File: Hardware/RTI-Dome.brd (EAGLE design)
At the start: 80 x 71.1 mm, 49 parts, among them IC1 24AA128ST, IC2 74LVC244, IC3 FT232RL, IC4 74ABT244, X13 PN61729-S

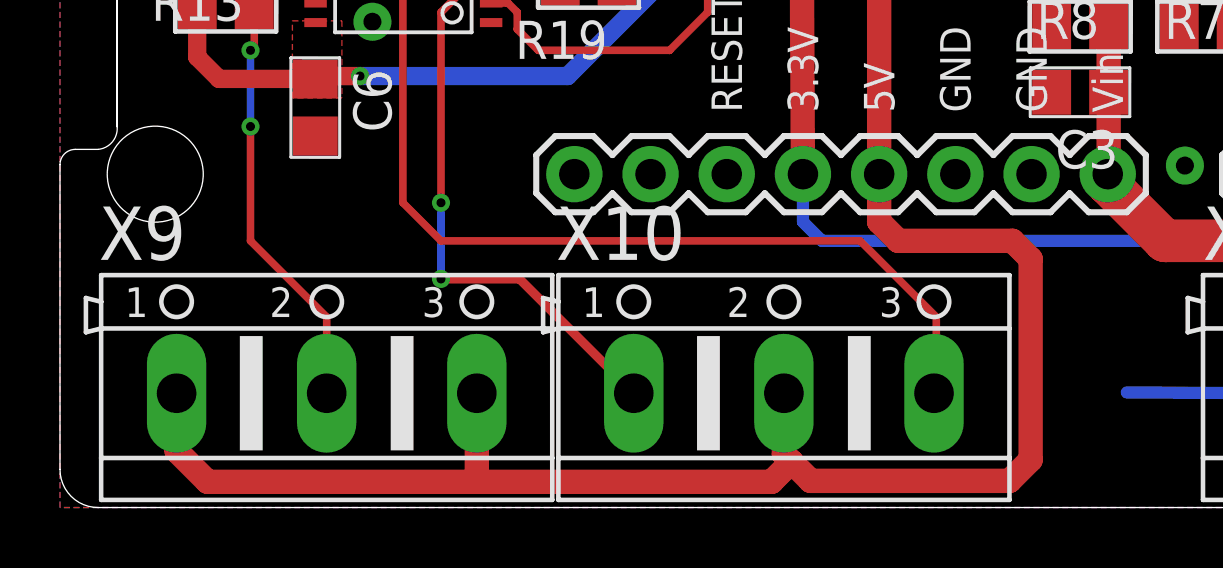
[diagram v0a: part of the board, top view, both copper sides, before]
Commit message: fix the stepper connection to match the TB6600 and work with the ISD02/04/08 controller with the same settings
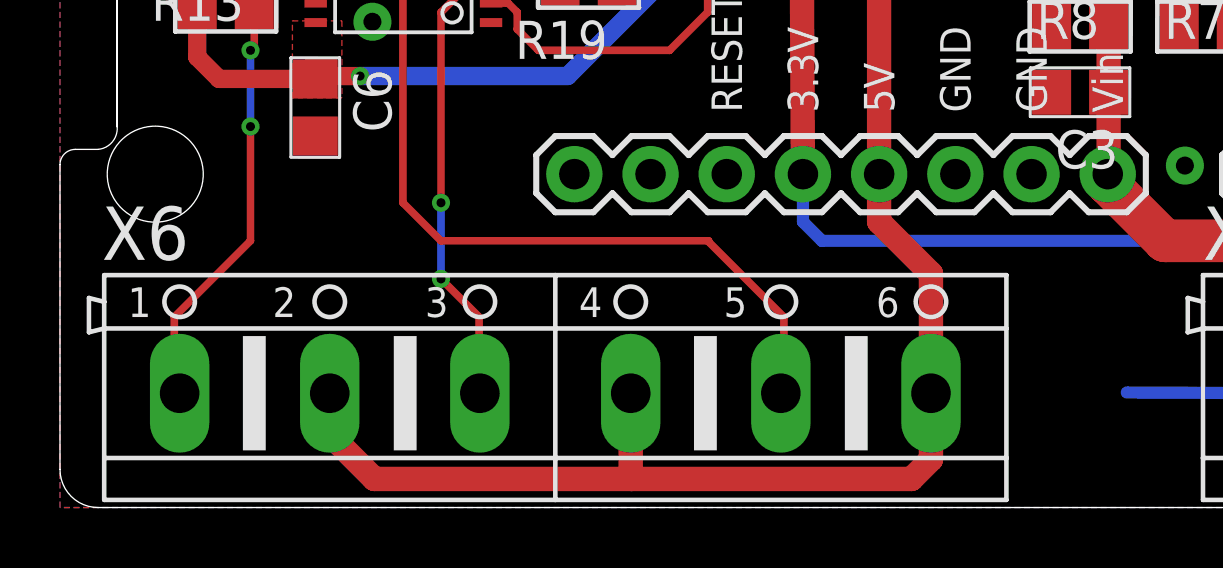
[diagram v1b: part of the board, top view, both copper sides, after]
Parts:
- removed X10, X9: (no value), con-ptr500:AK500/3
- added X6: (no value), con-ptr500:AK500/6
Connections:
- net M_DIR_5V: now also X6.3; no longer X10.1
- net M_EN_5V: now also X6.1; no longer X9.2
- net M_STEP_5V: now also X6.5; no longer X10.3
- net VCC: now also X6.2, X6.4, X6.6; no longer X10.2, X9.1, X9.3
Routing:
- net VCC: track 178.2 -> 162.8 mm
- net M_STEP_5V: track 34.9 -> 29.9 mm
- net M_DIR_5V: track 21.3 -> 17.6 mm
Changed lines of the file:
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@@
 <attribute name="OC_FARNELL" value="unknown" x="6.35" y="66.04" size="1.778" layer="27" rot="R180" display="off"/>
-</element>
-<element name="X9" library="con-ptr500" package="AK500/3" value="" x="8.89" y="3.81">
-<attribute name="MPN" value="" x="8.89" y="3.81" size="1.778" layer="27" display="off"/>
-<attribute name="MF" value="" x="8.89" y="3.81" size="1.778" layer="27" display="off"/>
-<attribute name="OC_NEWARK" value="unknown" x="8.89" y="3.81" size="1.778" layer="27" display="off"/>
-<attribute name="OC_FARNELL" value="unknown" x="8.89" y="3.81" size="1.778" layer="27" display="off"/>
-</element>
-<element name="X10" library="con-ptr500" package="AK500/3" value="" x="24.13" y="3.81">
-<attribute name="MPN" value="" x="24.13" y="3.81" size="1.778" layer="27" display="off"/>
-<attribute name="MF" value="" x="24.13" y="3.81" size="1.778" layer="27" display="off"/>
-<attribute name="OC_NEWARK" value="unknown" x="24.13" y="3.81" size="1.778" layer="27" display="off"/>
-<attribute name="OC_FARNELL" value="unknown" x="24.13" y="3.81" size="1.778" layer="27" display="off"/>
 </element>
 <element name="X11" library="con-ptr500" package="AK500/2" value="" x="60.96" y="3.81">
@@
 <element name="C9" library="rti" package="C0805" value="100nF" x="60.833" y="24.73325" rot="R270"/>
 <element name="R21" library="rti" package="R0805" value="4.7K" x="39.6875" y="43.18" rot="R270"/>
+<element name="X6" library="con-ptr500" package="AK500/6" value="" x="16.51" y="3.81">
+<attribute name="OC_NEWARK" value="unknown" x="16.51" y="3.81" size="1.778" layer="27" display="off"/>
+<attribute name="OC_FARNELL" value="unknown" x="16.51" y="3.81" size="1.778" layer="27" display="off"/>
+<attribute name="MF" value="" x="16.51" y="3.81" size="1.778" layer="27" display="off"/>
+<attribute name="MPN" value="" x="16.51" y="3.81" size="1.778" layer="27" display="off"/>
+</element>
 </elements>
 <signals>
@@
 <signal name="M_STEP_5V">
 <contactref element="R13" pad="1"/>
-<contactref element="X10" pad="3"/>
 <contactref element="IC4" pad="P$16"/>
 <wire x1="6.44275" y1="18.76425" x2="8.51925" y2="18.76425" width="0.254" layer="1"/>
@@
 <wire x1="11.43" y1="17.78" x2="11.43" y2="10.16" width="0.254" layer="1"/>
 <wire x1="11.43" y1="10.16" x2="12.7" y2="8.89" width="0.254" layer="1"/>
-<wire x1="12.7" y1="8.89" x2="26.67" y2="8.89" width="0.254" layer="1"/>
-<wire x1="26.67" y1="8.89" x2="29.21" y2="6.35" width="0.254" layer="1"/>
-<wire x1="29.21" y1="6.35" x2="29.21" y2="3.8862" width="0.254" layer="1"/>
-<wire x1="29.21" y1="3.8862" x2="29.1338" y2="3.81" width="0.254" layer="1"/>
+<wire x1="12.7" y1="8.89" x2="21.59" y2="8.89" width="0.254" layer="1"/>
+<contactref element="X6" pad="5"/>
+<wire x1="21.59" y1="8.89" x2="21.62175" y2="8.89" width="0.254" layer="1"/>
+<wire x1="21.62175" y1="8.89" x2="21.62175" y2="8.85825" width="0.254" layer="1"/>
+<wire x1="21.62175" y1="8.85825" x2="24.13" y2="6.35" width="0.254" layer="1"/>
+<wire x1="24.13" y1="6.35" x2="24.13" y2="3.9116" width="0.254" layer="1"/>
+<wire x1="24.13" y1="3.9116" x2="24.0284" y2="3.81" width="0.254" layer="1"/>
 </signal>
 <signal name="M_DIR_5V">
 <contactref element="R19" pad="2"/>
-<contactref element="X10" pad="1"/>
 <contactref element="IC4" pad="P$3"/>
 <wire x1="14.37" y1="17.465" x2="16.642" y2="17.465" width="0.254" layer="1"/>
 <wire x1="16.642" y1="17.465" x2="16.67125" y2="17.49425" width="0.254" layer="1"/>
-<wire x1="19.1262" y1="3.81" x2="19.05" y2="3.81" width="0.254" layer="1"/>
 <via x="12.7" y="7.62" extent="1-16" drill="0.3"/>
 <wire x1="12.7" y1="7.62" x2="12.7" y2="10.16" width="0.254" layer="16"/>
@@
 <wire x1="14.37" y1="17.465" x2="13.655" y2="17.465" width="0.254" layer="1"/>
 <wire x1="13.655" y1="17.465" x2="12.7" y2="16.51" width="0.254" layer="1"/>
-<wire x1="12.7" y1="7.62" x2="15.3162" y2="7.62" width="0.3048" layer="1"/>
-<wire x1="15.3162" y1="7.62" x2="19.1262" y2="3.81" width="0.3048" layer="1"/>
+<contactref element="X6" pad="3"/>
+<wire x1="12.7" y1="7.62" x2="13.97" y2="6.35" width="0.254" layer="1"/>
+<wire x1="13.97" y1="6.35" x2="13.97" y2="3.8354" width="0.254" layer="1"/>
+<wire x1="13.97" y1="3.8354" x2="13.9954" y2="3.81" width="0.254" layer="1"/>
 </signal>
 <signal name="M_EN_5V">
 <contactref element="R14" pad="2"/>
-<contactref element="X9" pad="2"/>
 <contactref element="IC4" pad="P$18"/>
 <wire x1="8.52" y1="17.465" x2="7.239" y2="17.465" width="0.254" layer="1"/>
@@
 <via x="6.35" y="12.7" extent="1-16" drill="0.3"/>
 <wire x1="6.35" y1="12.7" x2="6.35" y2="8.89" width="0.254" layer="1"/>
-<wire x1="6.35" y1="8.89" x2="8.89" y2="6.35" width="0.254" layer="1"/>
-<wire x1="8.89" y1="6.35" x2="8.89" y2="3.81" width="0.254" layer="1"/>
+<contactref element="X6" pad="1"/>
+<wire x1="6.35" y1="8.89" x2="3.81" y2="6.35" width="0.254" layer="1"/>
+<wire x1="3.81" y1="6.35" x2="3.81" y2="3.9878" width="0.254" layer="1"/>
+<wire x1="3.81" y1="3.9878" x2="3.9878" y2="3.81" width="0.254" layer="1"/>
 </signal>
 <signal name="RG-11-IN_EXT">
@@
 <via x="39.6875" y="45.72" extent="1-16" drill="0.3"/>
 <wire x1="39.6875" y1="45.72" x2="39.6875" y2="44.13" width="0.8128" layer="1"/>
-<contactref element="X9" pad="3"/>
-<contactref element="X9" pad="1"/>
-<contactref element="X10" pad="2"/>
-<wire x1="24.13" y1="3.81" x2="24.13" y2="1.778" width="0.8128" layer="1"/>
-<wire x1="24.13" y1="1.778" x2="24.384" y2="1.524" width="0.8128" layer="1"/>
-<wire x1="24.384" y1="1.524" x2="25.019" y2="0.889" width="0.8128" layer="1"/>
-<wire x1="25.019" y1="0.889" x2="31.65475" y2="0.889" width="0.8128" layer="1"/>
-<wire x1="31.65475" y1="0.889" x2="32.35325" y2="1.5875" width="0.8128" layer="1"/>
-<wire x1="3.8862" y1="3.81" x2="3.8862" y2="1.8923" width="0.8128" layer="1"/>
-<wire x1="3.8862" y1="1.8923" x2="4.92125" y2="0.85725" width="0.8128" layer="1"/>
-<wire x1="4.92125" y1="0.85725" x2="13.97" y2="0.85725" width="0.8128" layer="1"/>
-<wire x1="13.97" y1="0.85725" x2="23.71725" y2="0.85725" width="0.8128" layer="1"/>
-<wire x1="23.71725" y1="0.85725" x2="24.384" y2="1.524" width="0.8128" layer="1"/>
-<wire x1="13.8938" y1="3.81" x2="13.8938" y2="0.93345" width="0.8128" layer="1"/>
-<wire x1="13.8938" y1="0.93345" x2="13.97" y2="0.85725" width="0.8128" layer="1"/>
 <wire x1="27.305" y1="11.1125" x2="27.305" y2="9.525" width="0.8128" layer="1"/>
-<wire x1="27.305" y1="9.525" x2="27.94" y2="8.89" width="0.8128" layer="1"/>
-<wire x1="27.94" y1="8.89" x2="31.75" y2="8.89" width="0.8128" layer="1"/>
-<wire x1="32.35325" y1="1.5875" x2="32.35325" y2="8.28675" width="0.8128" layer="1"/>
-<wire x1="32.35325" y1="8.28675" x2="31.75" y2="8.89" width="0.8128" layer="1"/>
+<contactref element="X6" pad="2"/>
+<contactref element="X6" pad="4"/>
+<contactref element="X6" pad="6"/>
+<wire x1="27.305" y1="9.525" x2="29.0322" y2="7.7978" width="0.8128" layer="1"/>
+<wire x1="29.0322" y1="7.7978" x2="29.0322" y2="3.81" width="0.8128" layer="1"/>
+<wire x1="29.0322" y1="3.81" x2="29.0322" y2="1.6002" width="0.8128" layer="1"/>
+<wire x1="29.0322" y1="1.6002" x2="28.3845" y2="0.9525" width="0.8128" layer="1"/>
+<wire x1="28.3845" y1="0.9525" x2="19.05" y2="0.9525" width="0.8128" layer="1"/>
+<wire x1="19.05" y1="0.9525" x2="10.4775" y2="0.9525" width="0.8128" layer="1"/>
+<wire x1="10.4775" y1="0.9525" x2="8.89" y2="2.54" width="0.8128" layer="1"/>
+<wire x1="8.89" y1="2.54" x2="8.89" y2="3.7084" width="0.8128" layer="1"/>
+<wire x1="8.89" y1="3.7084" x2="8.9916" y2="3.81" width="0.8128" layer="1"/>
+<wire x1="19.0246" y1="3.81" x2="19.0246" y2="0.9779" width="0.8128" layer="1"/>
+<wire x1="19.0246" y1="0.9779" x2="19.05" y2="0.9525" width="0.8128" layer="1"/>
 </signal>
 <signal name="N$2">

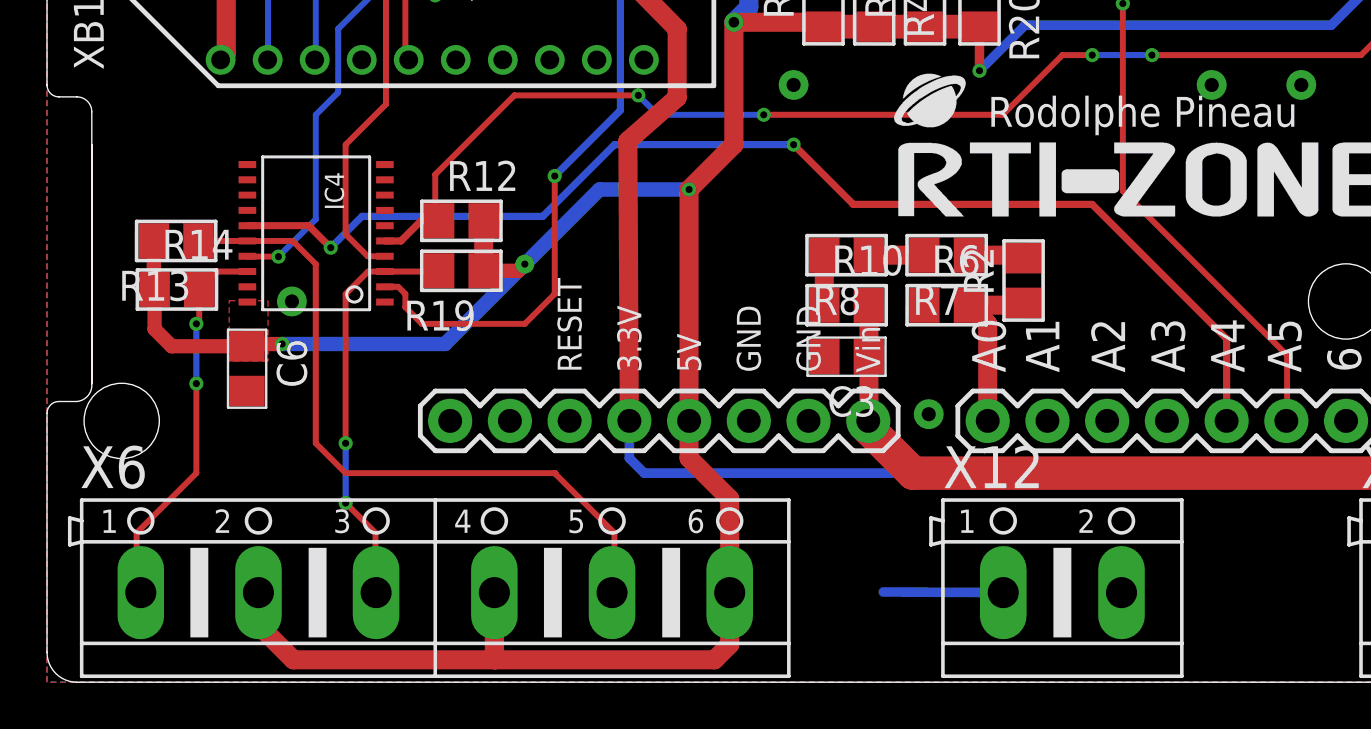
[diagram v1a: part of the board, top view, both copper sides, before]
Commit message: rewire the 74ABT244 to help with routing
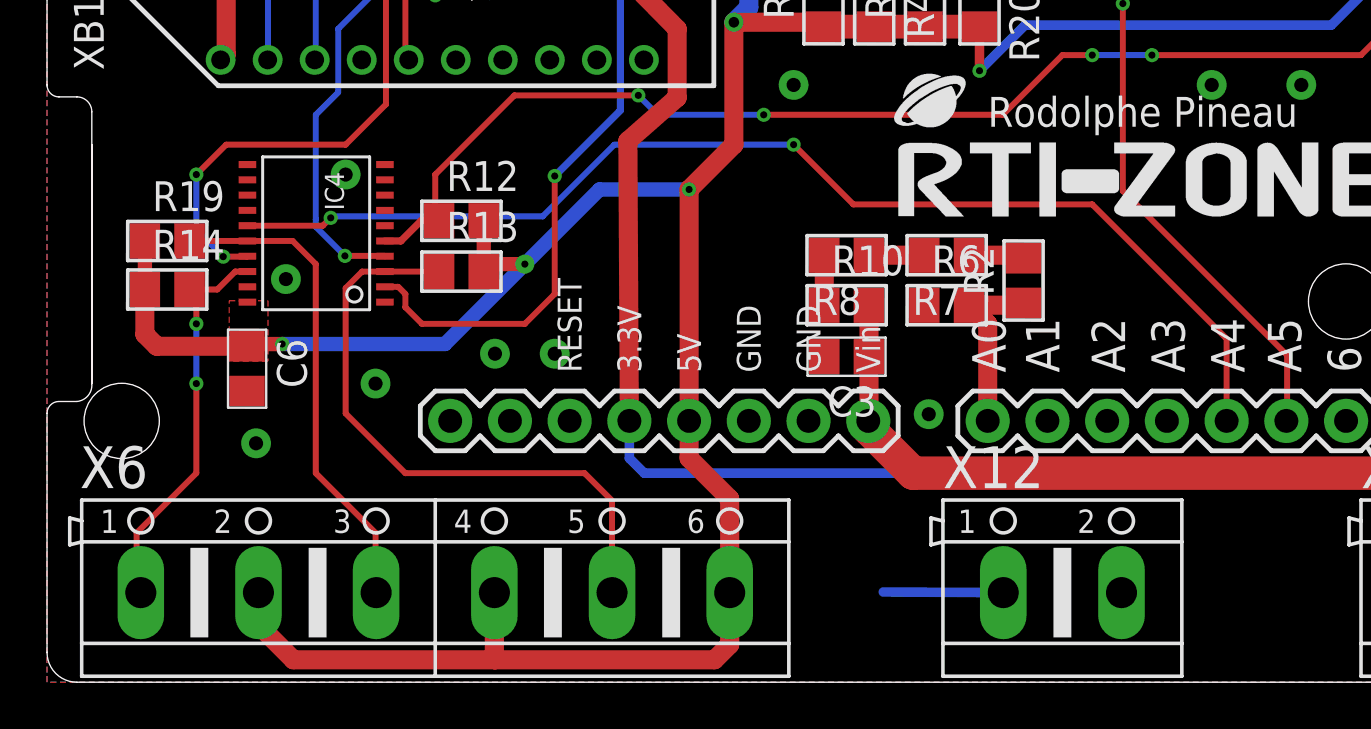
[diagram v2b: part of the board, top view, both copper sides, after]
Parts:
- moved R19 12.6 mm to (5.11, 18.8), turned to 0 degrees
- moved R13 12.2 mm to (17.6, 17.5), turned to 0 degrees
- moved R14 0.41 mm to (5.11, 16.7)
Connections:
- net M_DIR: now also IC4.P$4; no longer IC4.P$17
- net M_DIR_5V: now also IC4.P$16; no longer IC4.P$3
- net M_STEP: now also IC4.P$17; no longer IC4.P$4
- net M_STEP_5V: now also IC4.P$3; no longer IC4.P$16
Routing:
- net M_STEP: track 47.1 -> 53.1 mm, vias 2 -> 4
- net M_STEP_5V: track 29.9 -> 26.4 mm
- net M_DIR_5V: track 17.6 -> 20.8 mm, vias 2 -> 0
- net M_EN_5V: track 16.4 -> 17.3 mm
- net AT_PARK_PIN_LOOP: track 50.8 -> 50.0 mm
- net VCC: track 162.8 -> 163.4 mm
- net GND: vias 31 -> 36

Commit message: Cleanup some signals, Added bigger polygone on both side for 12V in and motor.
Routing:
- net GND: track 5.11 -> 0.00 mm, vias 36 -> 42
- net 3.3V: track 139.6 -> 138.1 mm
- net +12V: vias 0 -> 32
- added copper zone on layer 16, net +12V
